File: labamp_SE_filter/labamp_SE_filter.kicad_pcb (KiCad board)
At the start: 2 copper layers, 55 x 26 mm, 13 parts, among them J1 Conn_02x06_Odd_Even, J2 Conn_02x06_Odd_Even, J3 Conn_01x03

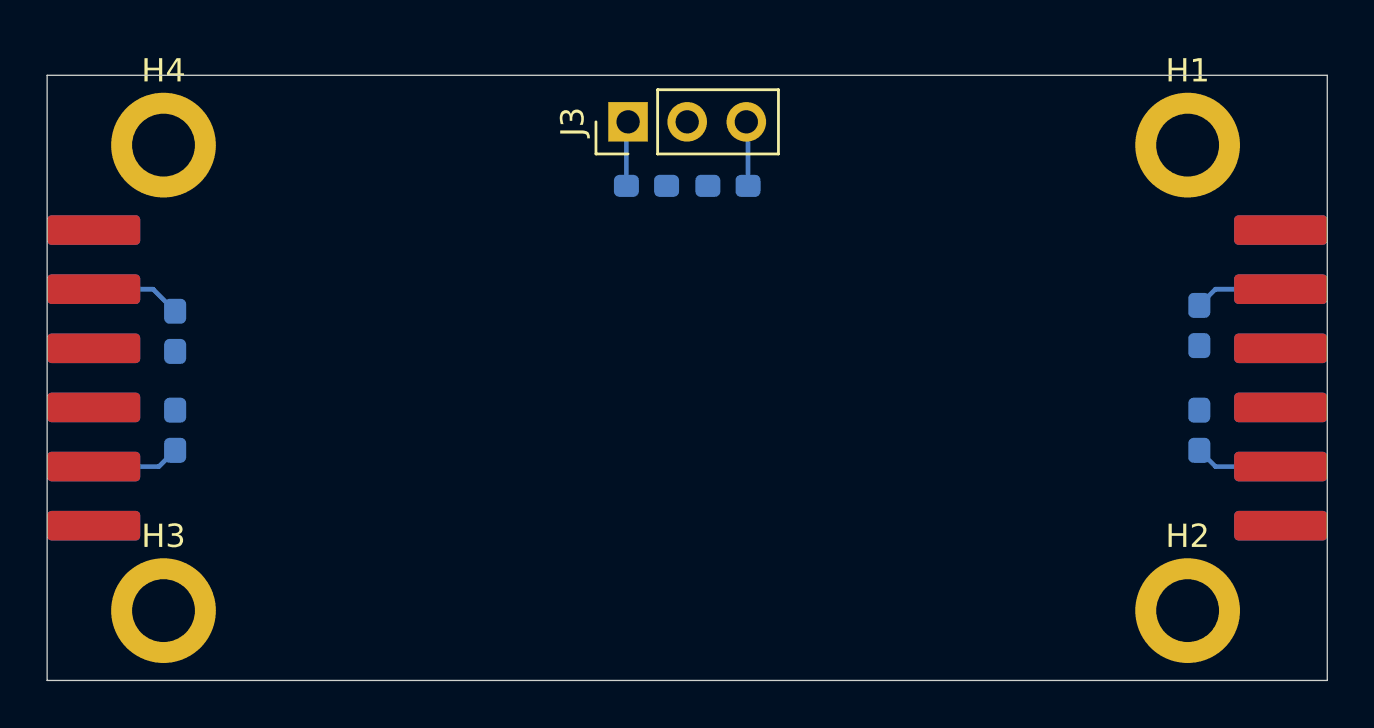
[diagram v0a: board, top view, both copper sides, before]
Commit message: Moved mounting holes to avoid colision with header
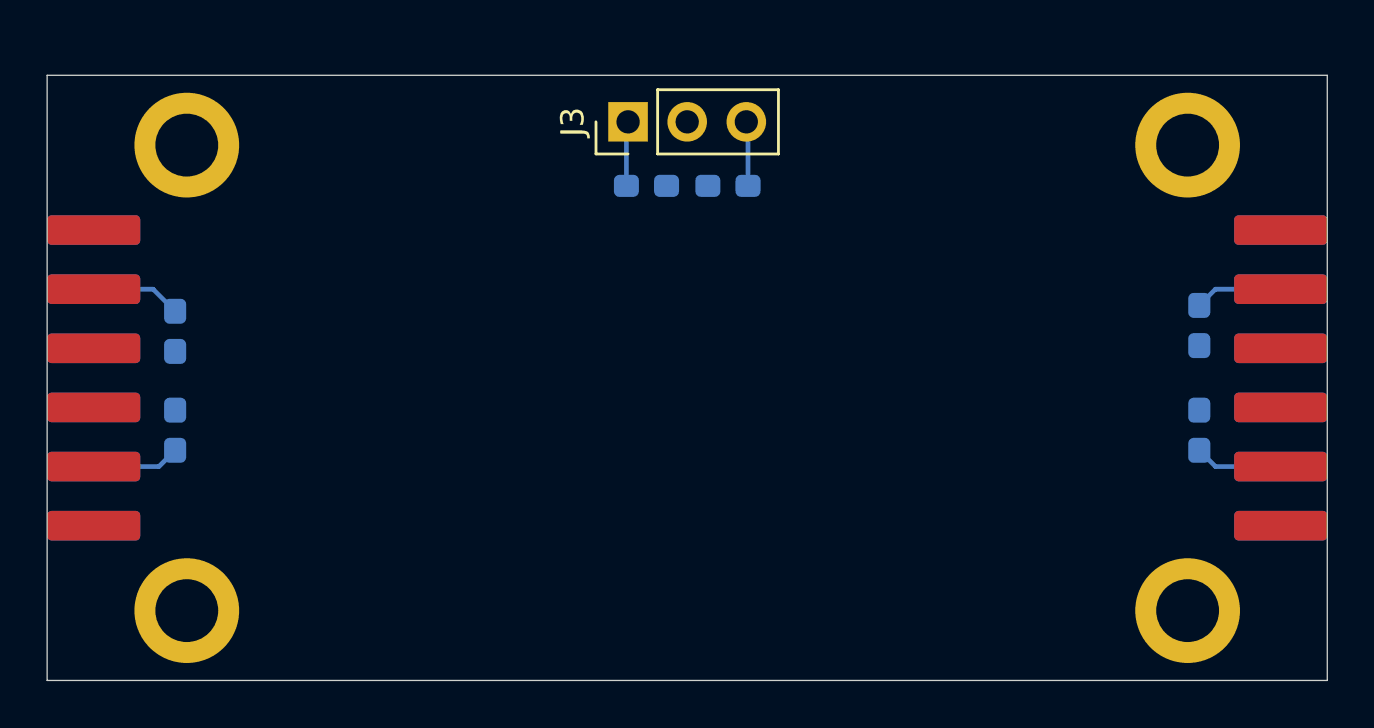
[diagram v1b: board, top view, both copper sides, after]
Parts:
- moved H3 1.00 mm to (101.0, 100.0)
- moved H4 1.00 mm to (101.0, 80.0)
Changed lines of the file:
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@@
 			(at 0 -3.2 0)
 			(layer "F.SilkS")
+			(hide yes)
 			(effects
 				(font
@@
 			(at 0 3.2 0)
 			(layer "F.Fab")
+			(hide yes)
 			(effects
 				(font
@@
 			(at 0 -3.2 0)
 			(layer "F.SilkS")
+			(hide yes)
 			(effects
 				(font
@@
 			(at 0 3.2 0)
 			(layer "F.Fab")
+			(hide yes)
 			(effects
 				(font
@@
 			(fill no)
 			(layer "F.CrtYd")
-		)
-		(fp_text user "${REFERENCE}"
-			(at 0 -3 0)
-			(layer "F.Fab")
-			(effects
-				(font
-					(size 1 1)
-					(thickness 0.15)
-				)
-			)
 		)
 		(pad "1" thru_hole circle
@@
 	(footprint "MountingHole:MountingHole_2.7mm_M2.5_ISO14580_Pad"
 		(layer "F.Cu")
-		(at 100 80)
+		(at 101 80)
 		(descr "Mounting Hole 2.7mm, M2.5, generated by kicad-footprint-generator mountinghole.py")
 		(tags "mountinghole M2.5 ISO14580")
@@
 			(at 0 -3.2 0)
 			(layer "F.SilkS")
+			(hide yes)
 			(effects
 				(font
@@
 			(at 1.5 9.55 180)
 			(layer "F.Fab")
+			(hide yes)
 			(effects
 				(font
@@
 	(footprint "MountingHole:MountingHole_2.7mm_M2.5_ISO14580_Pad"
 		(layer "F.Cu")
-		(at 100 100)
+		(at 101 100)
 		(descr "Mounting Hole 2.7mm, M2.5, generated by kicad-footprint-generator mountinghole.py")
 		(tags "mountinghole M2.5 ISO14580")
@@
 			(at 0 -3.2 0)
 			(layer "F.SilkS")
+			(hide yes)
 			(effects
 				(font
@@
 			(at 0 3.2 0)
 			(layer "F.Fab")
-			(effects
-				(font
+			(hide yes)
+			(effects
+				(font

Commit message: SE filter routed 90%
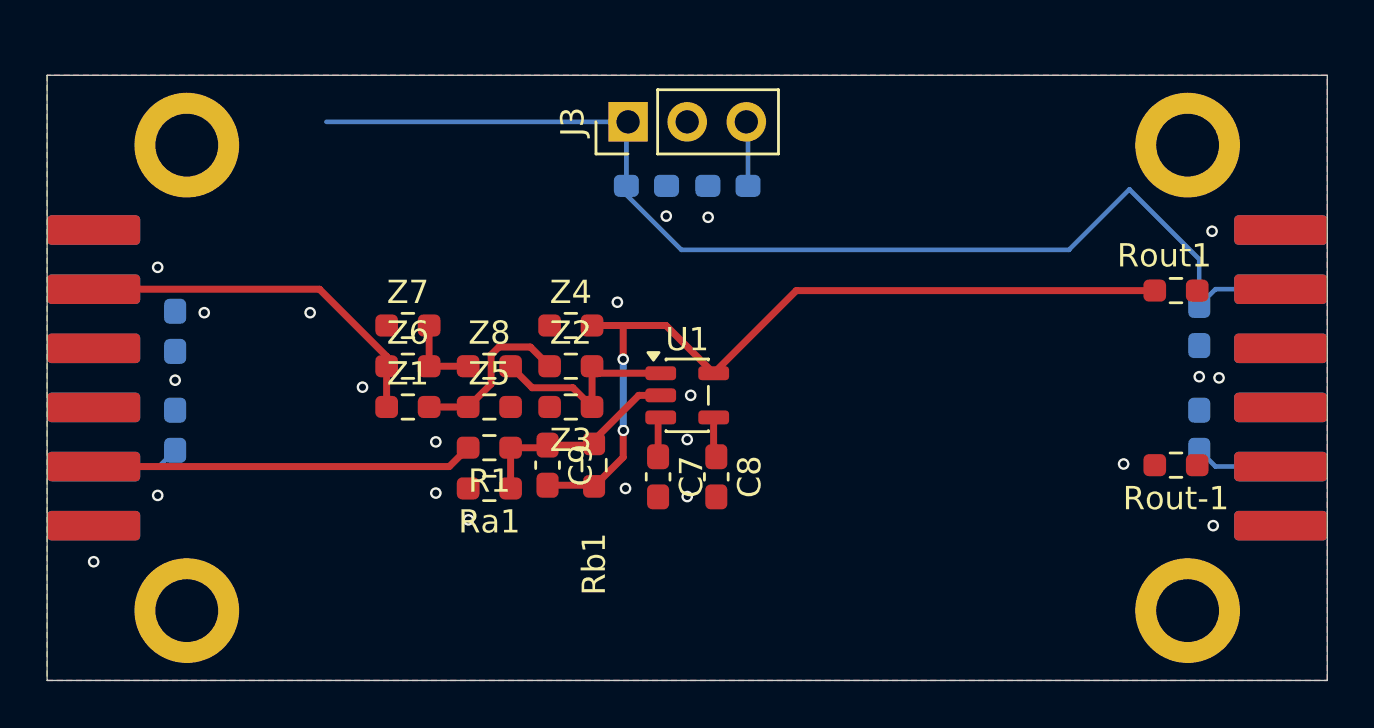
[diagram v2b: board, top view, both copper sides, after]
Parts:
- added C7: 100nF, Capacitor_SMD:C_0603_1608Metric_Pad1.08x0.95mm_HandSolder, F.Cu at (121.2, 94.2)
- added C8: 100nF, Capacitor_SMD:C_0603_1608Metric_Pad1.08x0.95mm_HandSolder, F.Cu at (123.8, 94.2)
- added C9: TBD, Capacitor_SMD:C_0603_1608Metric_Pad1.08x0.95mm_HandSolder, F.Cu at (116.5, 93.8)
- added R1: R, Resistor_SMD:R_0603_1608Metric_Pad0.98x0.95mm_HandSolder, F.Cu at (114.0, 93.0)
- added Ra1: R, Resistor_SMD:R_0603_1608Metric_Pad0.98x0.95mm_HandSolder, F.Cu at (114.0, 94.8)
- added Rb1: R, Resistor_SMD:R_0603_1608Metric_Pad0.98x0.95mm_HandSolder, F.Cu at (118.5, 93.8)
- added Rout-1: R, Resistor_SMD:R_0603_1608Metric_Pad0.98x0.95mm_HandSolder, F.Cu at (143.5, 93.8)
- added Rout1: R, Resistor_SMD:R_0603_1608Metric_Pad0.98x0.95mm_HandSolder, F.Cu at (143.5, 86.2)
- added U1: ~, Package_TO_SOT_SMD:SOT-23-5, F.Cu at (122.5, 90.8)
- added Z1: R, Resistor_SMD:R_0603_1608Metric_Pad0.98x0.95mm_HandSolder, F.Cu at (110.5, 91.2)
- added Z2: R, Resistor_SMD:R_0603_1608Metric_Pad0.98x0.95mm_HandSolder, F.Cu at (117.5, 89.5)
- added Z3: R, Resistor_SMD:R_0603_1608Metric_Pad0.98x0.95mm_HandSolder, F.Cu at (117.5, 91.2)
- added Z4: R, Resistor_SMD:R_0603_1608Metric_Pad0.98x0.95mm_HandSolder, F.Cu at (117.5, 87.8)
- added Z5: R, Resistor_SMD:R_0603_1608Metric_Pad0.98x0.95mm_HandSolder, F.Cu at (114.0, 91.2)
- added Z6: R, Resistor_SMD:R_0603_1608Metric_Pad0.98x0.95mm_HandSolder, F.Cu at (110.5, 89.5)
- added Z7: R, Resistor_SMD:R_0603_1608Metric_Pad0.98x0.95mm_HandSolder, F.Cu at (110.5, 87.8)
- added Z8: R, Resistor_SMD:R_0603_1608Metric_Pad0.98x0.95mm_HandSolder, F.Cu at (114.0, 89.5)
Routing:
- net +3.3V: track 10.6 -> 51.7 mm
- net Net-(C9-Pad2): track 0.00 -> 36.0 mm, vias 0 -> 2
- net /in-: track 0.00 -> 16.4 mm
- net /in+: track 0.00 -> 16.0 mm
- net Net-(U1--): track 0.00 -> 9.23 mm
- net Net-(U1-+): track 0.00 -> 9.05 mm
- net Net-(Z1-Pad2): track 0.00 -> 7.32 mm
- net Net-(Z6-Pad2): track 0.00 -> 3.43 mm
- net -3V3: track 10.6 -> 12.3 mm
- net GND: vias 0 -> 22
- added copper zone on B.Cu, net GND
- added copper zone on F.Cu, net GND

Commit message: Finished routing
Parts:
- moved R1 1.60 mm to (114.0, 94.6)
- moved Ra1 1.35 mm to (114.0, 96.1)
- renumbered Rout-1 to R2, Rout1 to R3
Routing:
- net -3V3: track 12.3 -> 82.8 mm, vias 0 -> 3
- net +3.3V: track 51.7 -> 76.1 mm, vias 0 -> 1
- net /out-: track 0.00 -> 3.61 mm
- net /out+: track 0.00 -> 3.61 mm
- net Net-(Z1-Pad2): track 7.32 -> 9.07 mm
- net Net-(U1--): track 9.23 -> 9.88 mm
- net GND: vias 22 -> 36

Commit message: Addedversion etc. in silkscreen
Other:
- board text added: "SE filter Ver 1.0 BHH"
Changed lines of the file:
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@@
 			(outputformat 1)
 			(mirror no)
-			(drillshape 1)
+			(drillshape 0)
 			(scaleselection 1)
-			(outputdirectory "")
+			(outputdirectory "labamp_SE_filter_fab/")
 		)
 	)
@@
 		(layer "Edge.Cuts")
 	)
+	(gr_text "SE filter\nVer 1.0\nBHH"
+		(at 134.1 84.5 0)
+		(layer "F.SilkS")
+		(effects
+			(font
+				(size 1.5 1.5)
+				(thickness 0.3)
+				(bold yes)
+			)
+			(justify bottom)
+		)
+	)
 	(via
